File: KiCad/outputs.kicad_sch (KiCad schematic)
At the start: 11 parts, among them J11 LED_Data, J12 LED_Data, U4 SN74LVC2T45DCUR, U5 SN74LVC2T45DCUR, U6 SN74LVC2T45DCUR

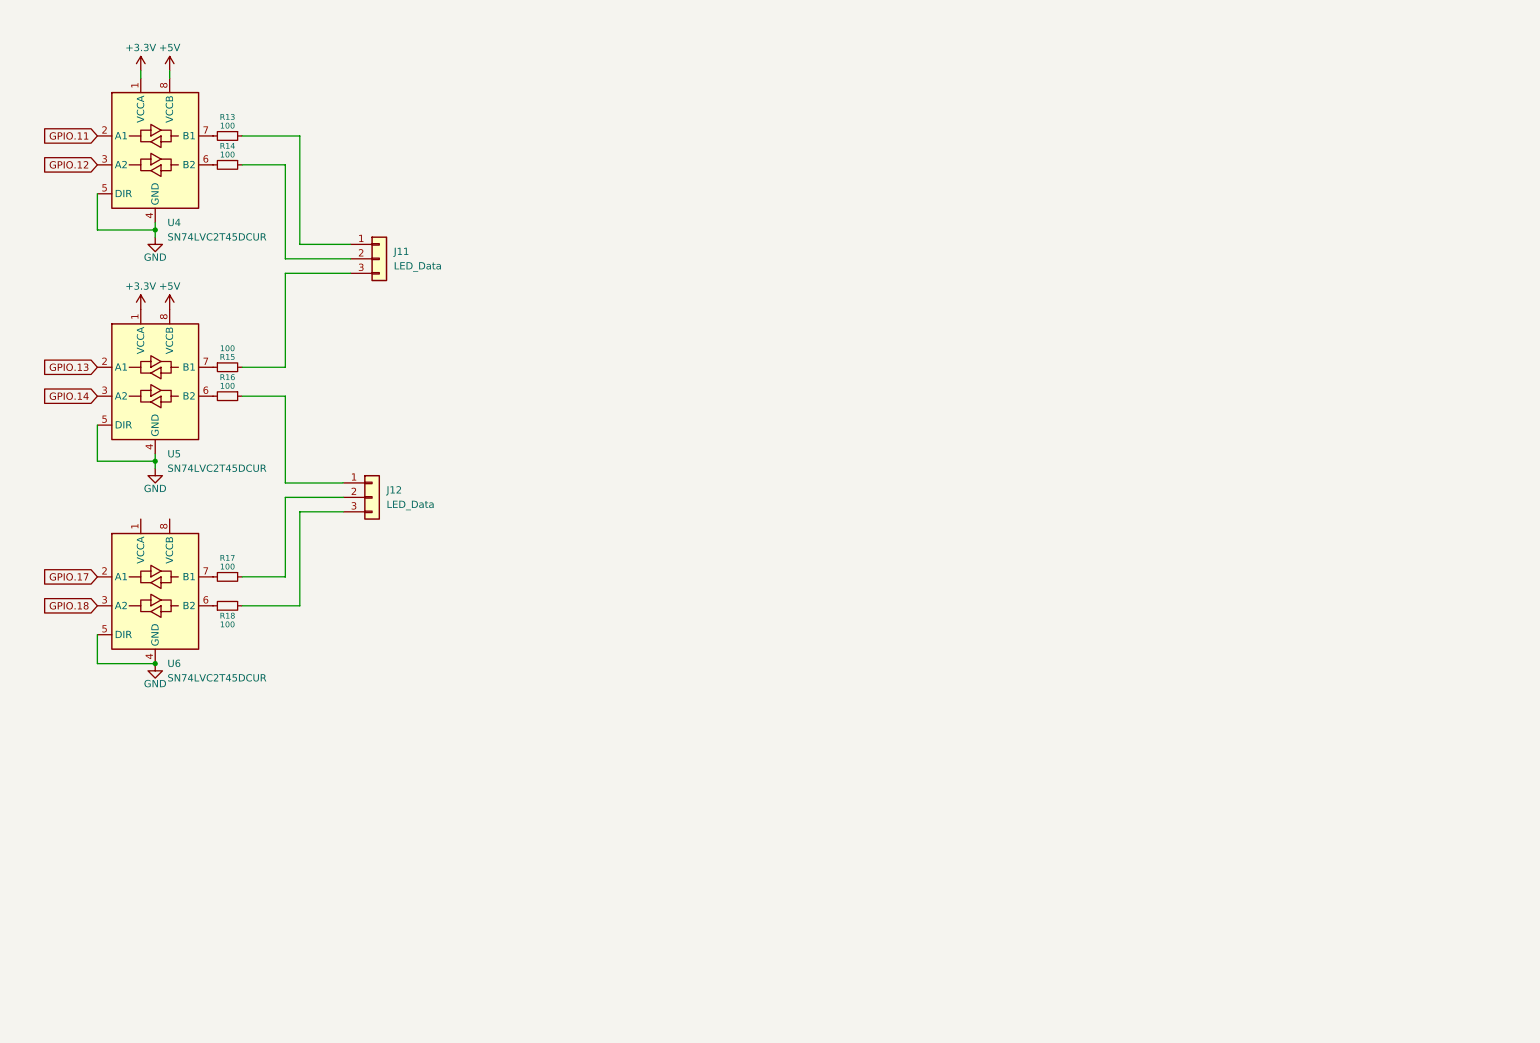
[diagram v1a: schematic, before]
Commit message: delete pwm, add 12 neopixel outputs
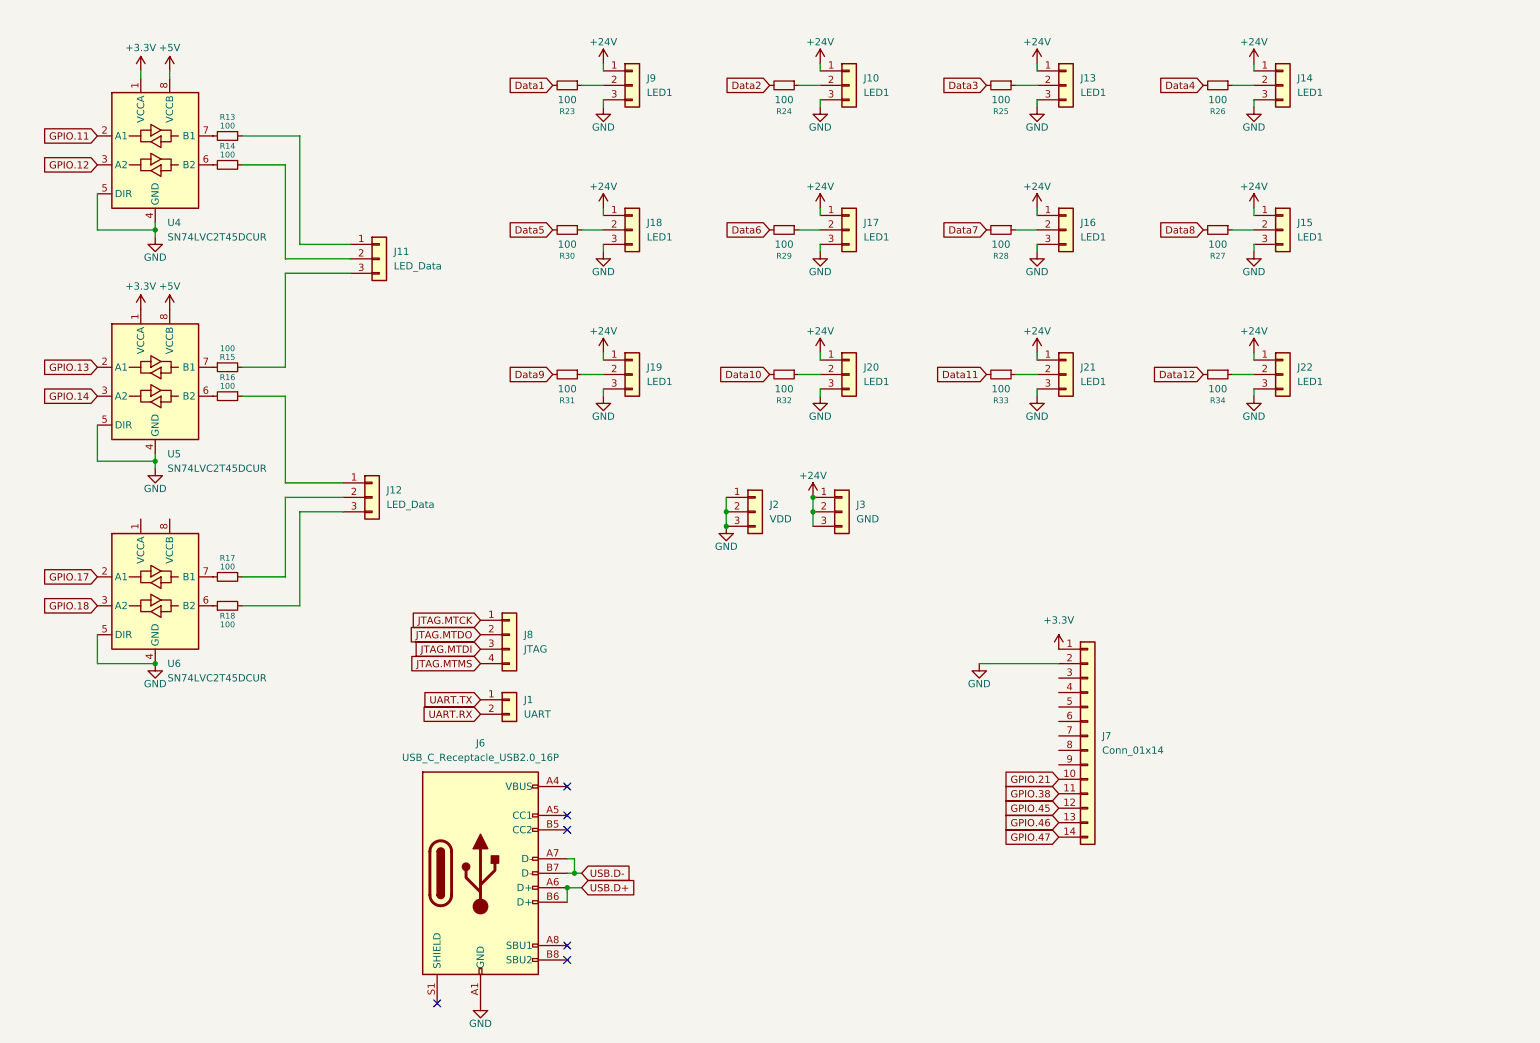
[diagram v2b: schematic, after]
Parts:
- added J1: UART, Connector_PinHeader_2.54mm:PinHeader_1x02_P2.54mm_Vertical, symbol Connector_Generic:Conn_01x02
- added J10, J13, J14, J15, J16, J17, J18, J19, J20, J21, J22, J9: LED1, Connector_JST:JST_XH_B3B-XH-A_1x03_P2.50mm_Vertical, symbol Connector_Generic:Conn_01x03
- added J2: VDD, TerminalBlock_Phoenix:TerminalBlock_Phoenix_MKDS-1,5-3-5.08_1x03_P5.08mm_Horizontal, symbol Connector_Generic:Conn_01x03
- added J3: GND, TerminalBlock_Phoenix:TerminalBlock_Phoenix_MKDS-1,5-3-5.08_1x03_P5.08mm_Horizontal, symbol Connector_Generic:Conn_01x03
- added J6: USB_C_Receptacle_USB2.0_16P, Connector_USB:USB_C_Receptacle_GCT_USB4105-xx-A_16P_TopMnt_Horizontal, symbol Connector:USB_C_Receptacle_USB2.0_16P
- added J7: Conn_01x14, Connector_PinHeader_2.54mm:PinHeader_1x14_P2.54mm_Vertical, symbol Connector_Generic:Conn_01x14
- added J8: JTAG, Connector_PinHeader_2.54mm:PinHeader_1x04_P2.54mm_Vertical, symbol Connector_Generic:Conn_01x04
- added R23, R24, R25, R26, R27, R28, R29, R30, R31, R32, R33, R34: 100, Resistor_SMD:R_0805_2012Metric_Pad1.20x1.40mm_HandSolder, symbol Device:R_Small
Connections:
- net +3.3V: now also J7.1 (Pin_1)
- net GND: now also J10.3 (Pin_3), J13.3 (Pin_3), J14.3 (Pin_3), J15.3 (Pin_3), J16.3 (Pin_3), J17.3 (Pin_3), J18.3 (Pin_3), J19.3 (Pin_3), J2.1 (Pin_1), J2.2 (Pin_2), J2.3 (Pin_3), J20.3 (Pin_3), J21.3 (Pin_3), J22.3 (Pin_3), J6.A1 (GND), J6.A12 (GND), J6.B1 (GND), J6.B12 (GND), J7.2 (Pin_2), J9.3 (Pin_3)
- new net: J9.2 (Pin_2), R23.1
- new net: J22.2 (Pin_2), R34.1
- new net: J21.2 (Pin_2), R33.1
- new net: J17.2 (Pin_2), R29.1
- new net: J6.A4 (VBUS), J6.A9 (VBUS), J6.B4 (VBUS), J6.B9 (VBUS)
- new net: J14.2 (Pin_2), R26.1
- new net: J20.2 (Pin_2), R32.1
- new net: J16.2 (Pin_2), R28.1
- new net: J19.2 (Pin_2), R31.1
- new net: J15.2 (Pin_2), R27.1
- new net: J18.2 (Pin_2), R30.1
- new net: J10.2 (Pin_2), R24.1
- new net: J13.2 (Pin_2), R25.1
- new net +24V: J10.1 (Pin_1), J13.1 (Pin_1), J14.1 (Pin_1), J15.1 (Pin_1), J16.1 (Pin_1), J17.1 (Pin_1), J18.1 (Pin_1), J19.1 (Pin_1), J20.1 (Pin_1), J21.1 (Pin_1), J22.1 (Pin_1), J3.1 (Pin_1), J3.2 (Pin_2), J3.3 (Pin_3), J9.1 (Pin_1)
- new net Data1: R23.2
- new net Data10: R32.2
- new net Data11: R33.2
- new net Data12: R34.2
- new net Data2: R24.2
- new net Data3: R25.2
- new net Data4: R26.2
- new net Data5: R30.2
- new net Data6: R29.2
- new net Data7: R28.2
- new net Data8: R27.2
- new net Data9: R31.2
- new net GPIO.21: J7.10 (Pin_10)
- new net GPIO.38: J7.11 (Pin_11)
- new net GPIO.45: J7.12 (Pin_12)
- new net GPIO.46: J7.13 (Pin_13)
- new net GPIO.47: J7.14 (Pin_14)
- new net JTAG.MTCK: J8.1 (Pin_1)
- new net JTAG.MTDI: J8.3 (Pin_3)
- new net JTAG.MTDO: J8.2 (Pin_2)
- new net JTAG.MTMS: J8.4 (Pin_4)
- new net UART.RX: J1.2 (Pin_2)
- new net UART.TX: J1.1 (Pin_1)
- new net USB.D+: J6.A6 (D+), J6.B6 (D+)
- new net USB.D-: J6.A7 (D-), J6.B7 (D-)
- no-connect marks 0 -> 6

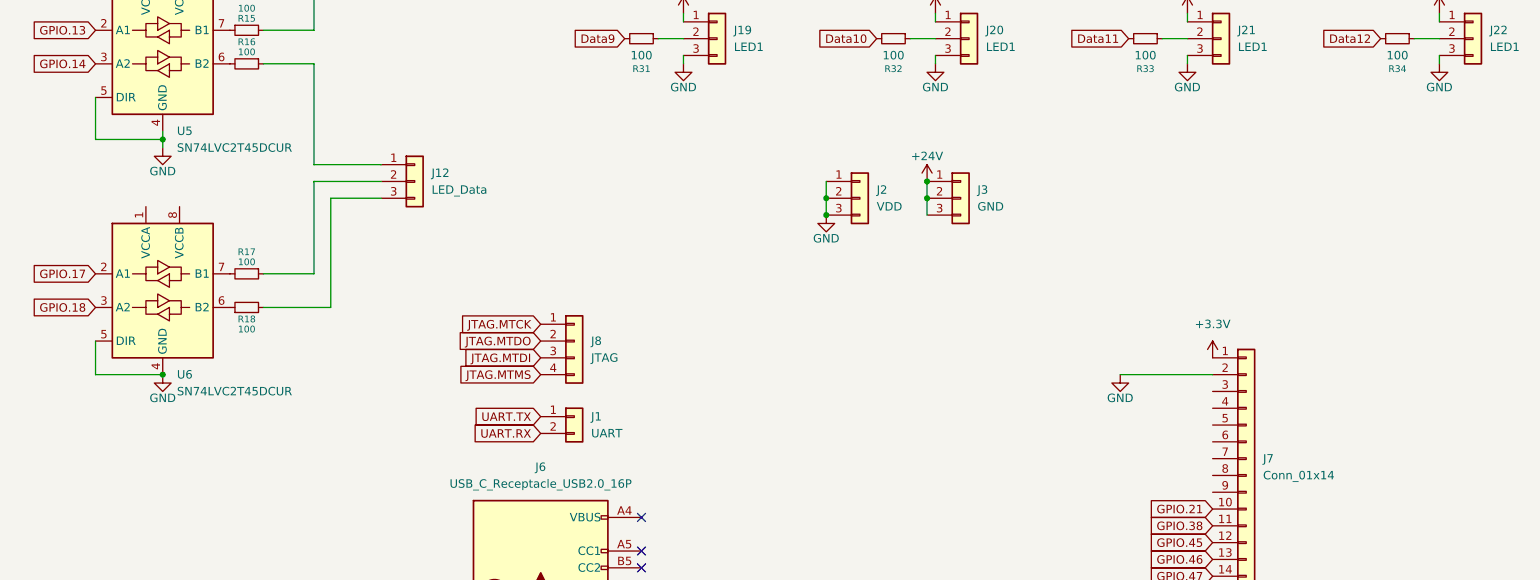
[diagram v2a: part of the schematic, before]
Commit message: add lcsc numbers
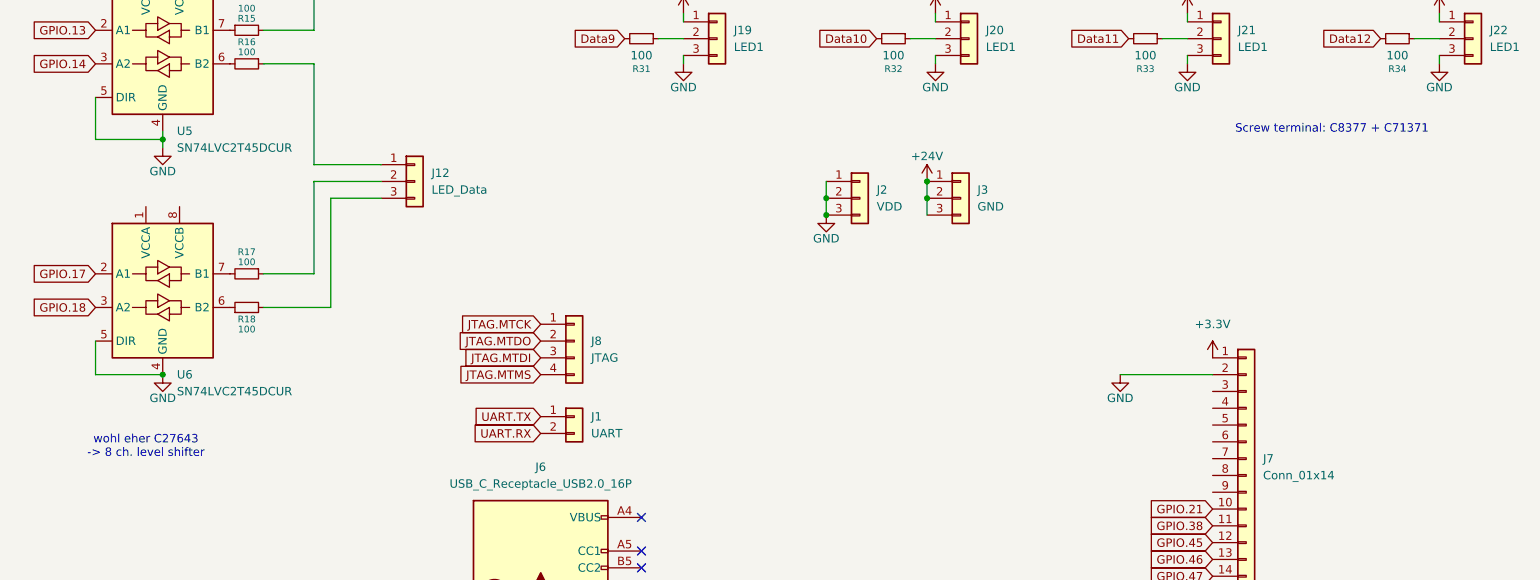
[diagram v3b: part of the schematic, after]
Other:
- note added: "Screw terminal: C8377 + C71371"
- note added: "wohl eher C27643 -> 8 ch. level shifter"
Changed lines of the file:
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@@
 	(generator_version "10.0")
 	(paper "A4")
+	(text "wohl eher C27643\n-> 8 ch. level shifter"
+		(exclude_from_sim no)
+		(at 41.91 137.922 0)
+		(effects
+			(font
+				(size 1.27 1.27)
+			)
+		)
+	)
+	(text "Screw terminal: C8377 + C71371"
+		(exclude_from_sim no)
+		(at 221.234 89.916 0)
+		(effects
+			(font
+				(size 1.27 1.27)
+			)
+		)
+	)
 	(junction
 		(at 160.02 100.33)

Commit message: work on new design
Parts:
- removed J11, J12: LED_Data, TerminalBlock_Phoenix:TerminalBlock_Phoenix_MKDS-1,5-3-5.08_1x03_P5.08mm_Horizontal, symbol Connector_Generic:Conn_01x03
- removed R13, R14, R15, R16, R17, R18, R23, R24, R25, R26, R27, R28, R29, R30, R31, R32, R33, R34: 100, Resistor_SMD:R_0805_2012Metric_Pad1.20x1.40mm_HandSolder, symbol Device:R_Small
- removed U4, U5, U6: SN74LVC2T45DCUR, Package_SO:VSSOP-8_2.3x2mm_P0.5mm, symbol Logic_LevelTranslator:SN74LVC2T45DCUR
- added R35, R36, R37, R38, R39, R40, R41, R42, R43, R44, R45, R46: 100, Resistor_SMD:R_0805_2012Metric_Pad1.20x1.40mm_HandSolder, symbol Device:R_Small
- added U7, U8: SN74LVC8T245, Package_SO:TSSOP-24_4.4x7.8mm_P0.65mm, symbol Logic_LevelTranslator:SN74LVC8T245
- J10: value LED1 -> LED2; footprint Connector_JST:JST_XH_B3B-XH-A_1x03_P2.50mm_Vertical -> TerminalBlock_Phoenix:TerminalBlock_Phoenix_MKDS-3-3-5.08_1x03_P5.08mm_Horizontal
- J13: value LED1 -> LED3; footprint Connector_JST:JST_XH_B3B-XH-A_1x03_P2.50mm_Vertical -> TerminalBlock_Phoenix:TerminalBlock_Phoenix_MKDS-3-3-5.08_1x03_P5.08mm_Horizontal
- J14: value LED1 -> LED4; footprint Connector_JST:JST_XH_B3B-XH-A_1x03_P2.50mm_Vertical -> TerminalBlock_Phoenix:TerminalBlock_Phoenix_MKDS-3-3-5.08_1x03_P5.08mm_Horizontal
- J15: value LED1 -> LED8; footprint Connector_JST:JST_XH_B3B-XH-A_1x03_P2.50mm_Vertical -> TerminalBlock_Phoenix:TerminalBlock_Phoenix_MKDS-3-3-5.08_1x03_P5.08mm_Horizontal
- J16: value LED1 -> LED7; footprint Connector_JST:JST_XH_B3B-XH-A_1x03_P2.50mm_Vertical -> TerminalBlock_Phoenix:TerminalBlock_Phoenix_MKDS-3-3-5.08_1x03_P5.08mm_Horizontal
- J17: value LED1 -> LED6; footprint Connector_JST:JST_XH_B3B-XH-A_1x03_P2.50mm_Vertical -> TerminalBlock_Phoenix:TerminalBlock_Phoenix_MKDS-3-3-5.08_1x03_P5.08mm_Horizontal
- J18: value LED1 -> LED5; footprint Connector_JST:JST_XH_B3B-XH-A_1x03_P2.50mm_Vertical -> TerminalBlock_Phoenix:TerminalBlock_Phoenix_MKDS-3-3-5.08_1x03_P5.08mm_Horizontal
- J19: value LED1 -> LED9; footprint Connector_JST:JST_XH_B3B-XH-A_1x03_P2.50mm_Vertical -> TerminalBlock_Phoenix:TerminalBlock_Phoenix_MKDS-3-3-5.08_1x03_P5.08mm_Horizontal
- J20: value LED1 -> LED10; footprint Connector_JST:JST_XH_B3B-XH-A_1x03_P2.50mm_Vertical -> TerminalBlock_Phoenix:TerminalBlock_Phoenix_MKDS-3-3-5.08_1x03_P5.08mm_Horizontal
- J21: value LED1 -> LED11; footprint Connector_JST:JST_XH_B3B-XH-A_1x03_P2.50mm_Vertical -> TerminalBlock_Phoenix:TerminalBlock_Phoenix_MKDS-3-3-5.08_1x03_P5.08mm_Horizontal
- J22: value LED1 -> LED12; footprint Connector_JST:JST_XH_B3B-XH-A_1x03_P2.50mm_Vertical -> TerminalBlock_Phoenix:TerminalBlock_Phoenix_MKDS-3-3-5.08_1x03_P5.08mm_Horizontal
- J9: footprint Connector_JST:JST_XH_B3B-XH-A_1x03_P2.50mm_Vertical -> TerminalBlock_Phoenix:TerminalBlock_Phoenix_MKDS-3-3-5.08_1x03_P5.08mm_Horizontal
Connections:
- net +24V: now also J2.1 (Pin_1), J2.2 (Pin_2), J2.3 (Pin_3); no longer J3.1 (Pin_1), J3.2 (Pin_2), J3.3 (Pin_3)
- net +3.3V: now also U7.1 (V_{CCA}), U7.2 (DIR), U8.1 (V_{CCA}), U8.2 (DIR)
- net +5V: now also U7.23 (V_{CCB}), U7.24 (V_{CCB}), U8.23 (V_{CCB}), U8.24 (V_{CCB})
- net Data1: now also U7.3 (A1)
- net Data10: now also U8.4 (A2)
- net Data11: now also U8.5 (A3)
- net Data12: now also U8.6 (A4)
- net Data2: now also U7.4 (A2)
- net Data3: now also U7.5 (A3)
- net Data4: now also U7.6 (A4)
- net Data5: now also U7.7 (A5)
- net Data6: now also U7.8 (A6)
- net Data7: now also U7.9 (A7)
- net Data8: now also U7.10 (A8)
- net Data9: now also U8.3 (A1)
- net GND: now also J3.1 (Pin_1), J3.2 (Pin_2), J3.3 (Pin_3), U7.11 (GND), U7.12 (GND), U7.13 (GND), U7.22 (~{OE}), U8.11 (GND), U8.12 (GND), U8.13 (GND), U8.22 (~{OE}); no longer J2.1 (Pin_1), J2.2 (Pin_2), J2.3 (Pin_3)
- net DataOut1: now reaches J9.2 (Pin_2)
- net DataOut1: now also R35.2
- net DataOut12: now reaches J22.2 (Pin_2)
- net DataOut12: now also R46.2
- net DataOut11: now reaches J21.2 (Pin_2)
- net DataOut11: now also R45.2
- net DataOut6: now reaches J17.2 (Pin_2)
- net DataOut6: now also R40.2
- net DataOut4: now reaches J14.2 (Pin_2)
- net DataOut4: now also R38.2
- net DataOut10: now reaches J20.2 (Pin_2)
- net DataOut10: now also R44.2
- net DataOut7: now reaches J16.2 (Pin_2)
- net DataOut7: now also R41.2
- net DataOut9: now reaches J19.2 (Pin_2)
- net DataOut9: now also R43.2
- net DataOut8: now reaches J15.2 (Pin_2)
- net DataOut8: now also R42.2
- net DataOut5: now reaches J18.2 (Pin_2)
- net DataOut5: now also R39.2
- net DataOut2: now reaches J10.2 (Pin_2)
- net DataOut2: now also R36.2
- net DataOut3: now reaches J13.2 (Pin_2)
- net DataOut3: now also R37.2
- new net: R35.1, U7.21 (B1)
- new net: R45.1, U8.19 (B3)
- new net: R36.1, U7.20 (B2)
- new net: R41.1, U7.15 (B7)
- new net: R46.1, U8.18 (B4)
- new net: R38.1, U7.18 (B4)
- new net: R37.1, U7.19 (B3)
- new net: R43.1, U8.21 (B1)
- new net: R44.1, U8.20 (B2)
- new net: R42.1, U7.14 (B8)
- new net: R40.1, U7.16 (B6)
- new net: R39.1, U7.17 (B5)
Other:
- note removed: "wohl eher C27643 -> 8 ch. level shifter"
- moved on the sheet: J1, J2, J3, J6, J8
